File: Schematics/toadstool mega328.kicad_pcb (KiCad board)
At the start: 2 copper layers, 49.5 x 81.2 mm, 26 parts, among them CON1 BARREL_JACK, IC1 ATMEGA328P-P, K1 SHIELD, K2 V-SELECT, K4 ICSP, K5 PIN 2-8, K6 PIN 21-28, K7 XTAL, K8 PIN 15-19, K9 PIN 11-14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

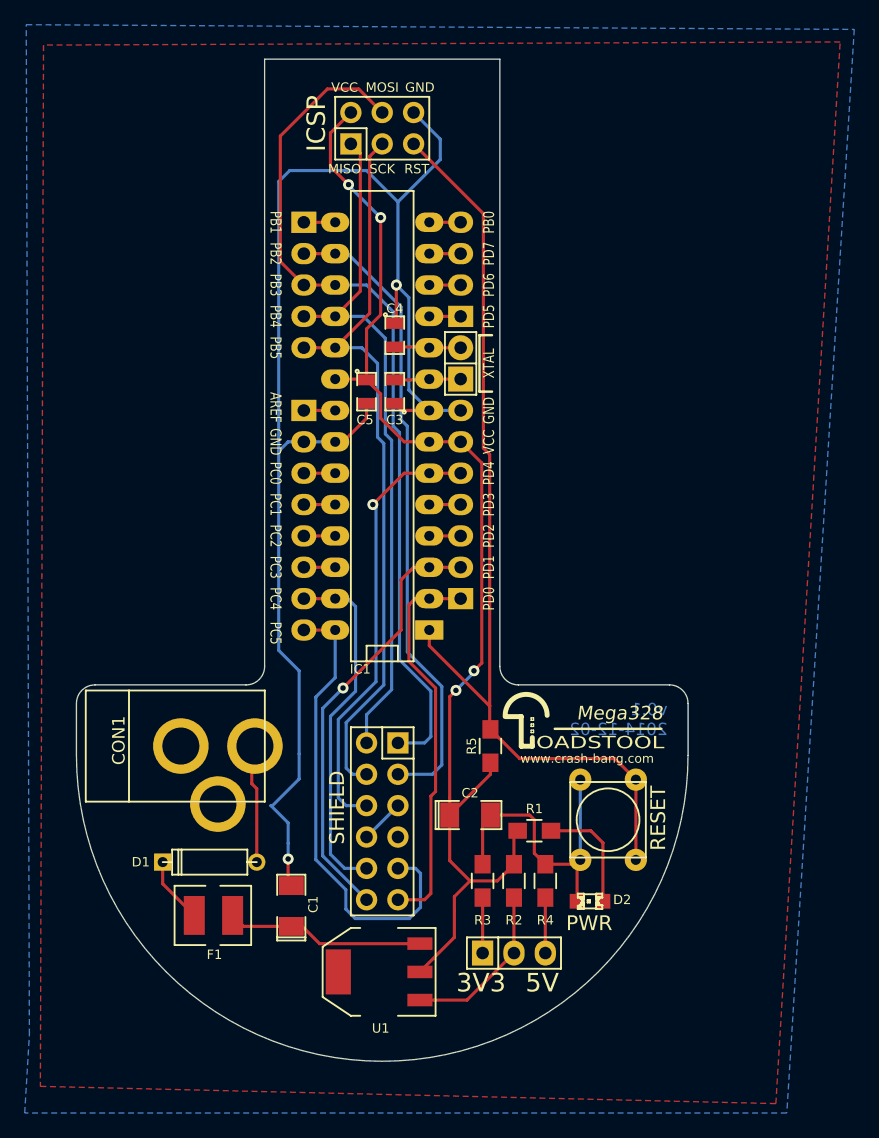
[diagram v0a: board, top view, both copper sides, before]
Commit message: Version 0.2 - Updates from v0.1 prototype
Final changes from v0.1 prototype:
- Add aluminium caps
- Silkscreen cosmetics
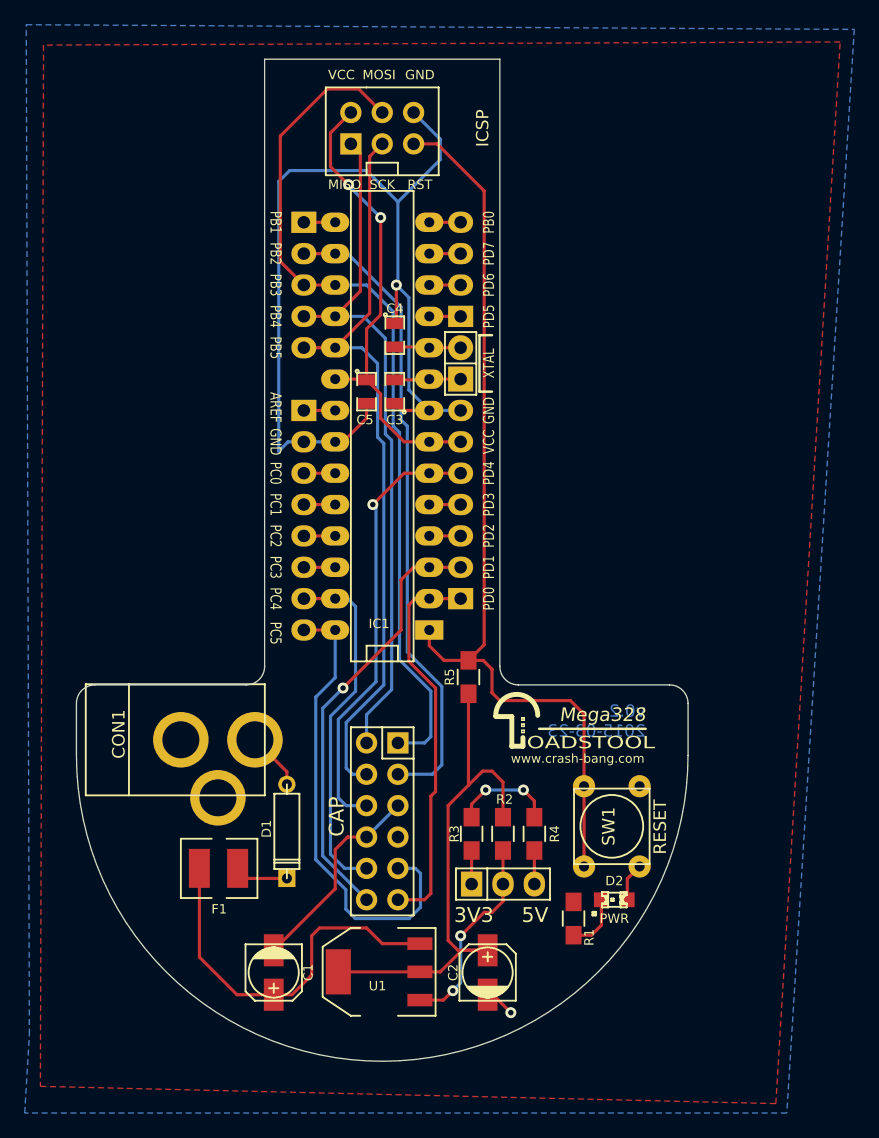
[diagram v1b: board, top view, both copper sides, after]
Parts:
- C1, C2: footprint SMD_Packages:SMD-1206_Pol -> toadstool:c_elec_4x5.3
- D2: footprint LEDs:LED-0805 -> Toadstool:LED-0805
- K1: value SHIELD -> CAP
- K4: footprint Pin_Headers:Pin_Header_Straight_2x03 -> Toadstool:ICSP_Header_2x03
- U1: footprint SMD_Packages:SOT-223 -> SOT-223
- moved C2 12.8 mm to (216.8, 121.7), turned to 90 degrees
- moved R1 7.79 mm to (223.8, 117.3), turned to 90 degrees
- moved D1 6.73 mm to (200.6, 110.3), turned to 270 degrees
- moved R5 5.86 mm to (215.3, 97.8)
- moved K2 5.66 mm to (218.1, 114.6)
- moved C1 5.57 mm to (199.5, 121.7), turned to 270 degrees
- moved R2 3.91 mm to (218.1, 110.5)
- moved R4 3.91 mm to (220.6, 110.5)
- moved R3 3.91 mm to (215.5, 110.5)
- moved F1 3.84 mm to (195.1, 113.3), turned to 0 degrees
- moved K4 2.84 mm to (205.7, 54.6), turned to 90 degrees
- moved D2 1.97 mm to (227.1, 115.8), turned to 0 degrees
- moved Toadstool_Logo 0.76 mm to (223.8, 101.1)
- moved SW1 0.61 mm to (226.9, 109.9), turned to 90 degrees
- moved CON1 0.51 mm to (191.8, 102.9)
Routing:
- net GND: track 144.7 -> 109.5 mm, vias 2 -> 4
- net VCC: track 98.3 -> 82.5 mm, vias 4 -> 2
- net Net-(C1-Pad1): track 16.4 -> 30.9 mm
- net Net-(CON1-Pad1): track 9.62 -> 4.68 mm
- net Net-(D2-Pad1): track 9.35 -> 4.97 mm
- net Net-(K2-Pad2): track 13.7 -> 16.9 mm, vias 0 -> 2
- net /RST: track 78.2 -> 75.4 mm
- net Net-(K2-Pad3): track 4.49 -> 2.71 mm
- net Net-(K2-Pad1): track 4.49 -> 2.71 mm
- net Net-(D1-Pad2): track 5.38 -> 4.32 mm
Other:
- board text added: "v0.2 2015-03-23"
- board text removed: "v0.1 2014-12-02"
